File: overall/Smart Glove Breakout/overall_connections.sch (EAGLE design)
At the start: 3 parts

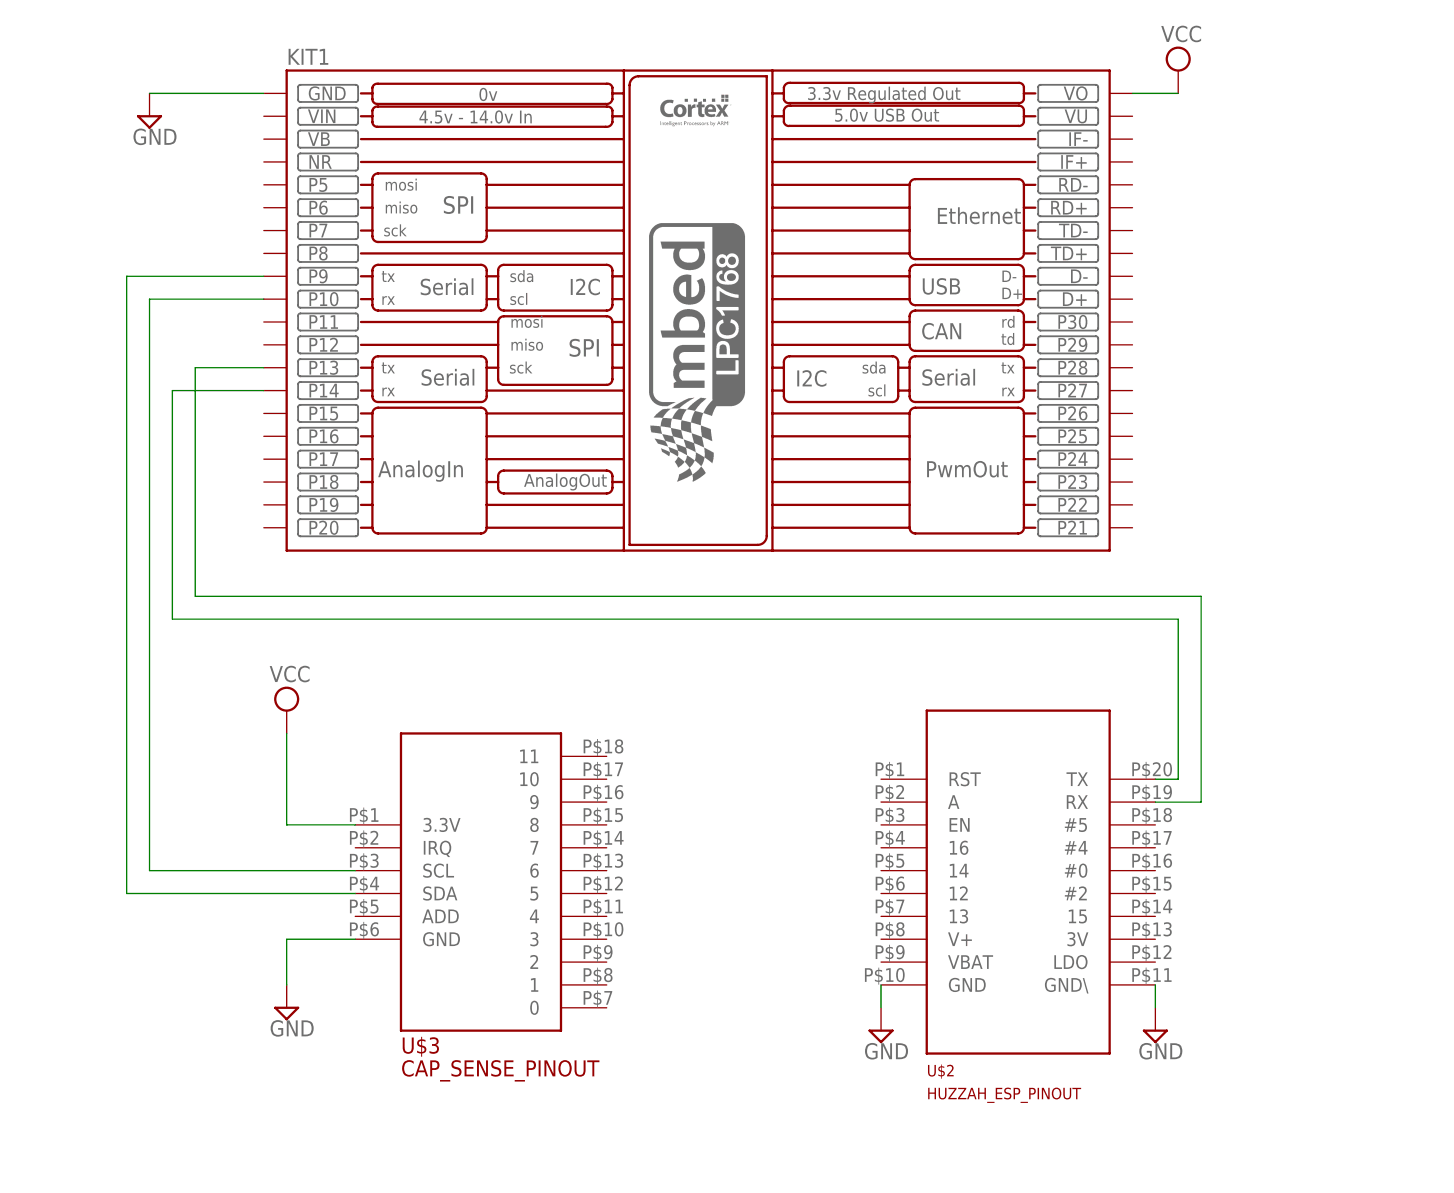
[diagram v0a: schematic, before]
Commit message: Revert "Started Board File"
This reverts commit 9f60d38fc5464a5e955318b8b377fab6b9ea1dbb.
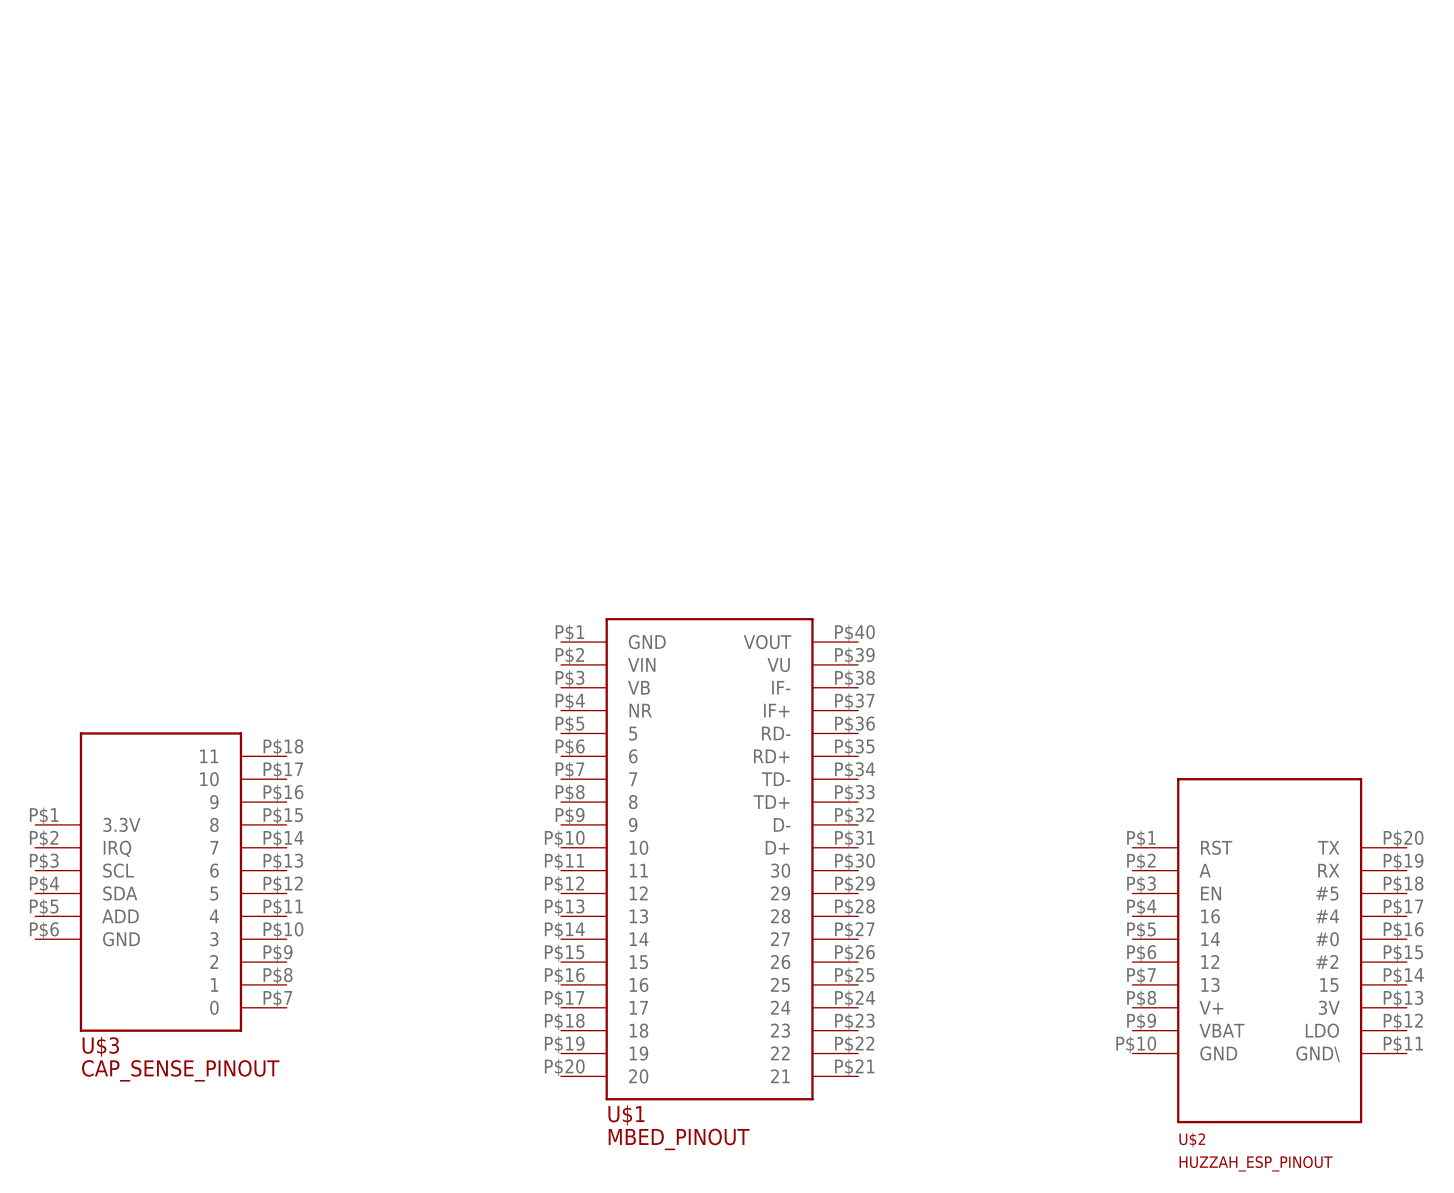
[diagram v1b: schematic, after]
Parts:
- removed KIT1: MBED_NXP_LPC1768, MBED_v2.1_avbotz:MBED_NXP_LPC1768
- added U$1: MBED_PINOUT, smart_glove_breakout:MBED_PINOUT
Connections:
- removed net GND: KIT1.GND, U$2.GND, U$2.GND\, U$3.GND
- removed net N$1: KIT1.P13, U$2.RX
- removed net N$2: KIT1.P14, U$2.TX
- removed net N$3: KIT1.P9, U$3.SDA
- removed net N$4: KIT1.P10, U$3.SCL
- removed net VCC: KIT1.VO, U$3.3.3V
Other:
- moved on the sheet: U$2, U$3
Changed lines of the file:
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@@
 <setting verticaltext="up"/>
 </settings>
-<grid distance="0.1" unitdist="inch" unit="inch" style="lines" multiple="1" display="no" altdistance="0.01" altunitdist="inch" altunit="inch"/>
+<grid distance="0.1" unitdist="inch" unit="inch" style="lines" multiple="1" display="yes" altdistance="0.01" altunitdist="inch" altunit="inch"/>
 <layers>
 <layer number="1" name="Top" color="4" fill="1" visible="no" active="no"/>
@@
 <layer number="97" name="Info" color="7" fill="1" visible="yes" active="yes"/>
 <layer number="98" name="Guide" color="6" fill="1" visible="yes" active="yes"/>
-<layer number="101" name="Hidden" color="15" fill="1" visible="no" active="yes"/>
-<layer number="102" name="Changes" color="12" fill="1" visible="no" active="yes"/>
 </layers>
 <schematic xreflabel="%F%N/%S.%C%R" xrefpart="/%S.%C%R">
@@
 </classes>
 <parts>
+<part name="U$1" library="smart_glove_breakout" deviceset="MBED_PINOUT" device=""/>
 <part name="U$2" library="smart_glove_breakout" deviceset="HUZZAH_ESP_PINOUT" device=""/>
 <part name="U$3" library="smart_glove_breakout" deviceset="CAP_SENSE_PINOUT" device=""/>
-<part name="KIT1" library="MBED_v2.1_avbotz" deviceset="MBED_NXP_LPC1768" device=""/>
-<part name="SUPPLY1" library="supply2" deviceset="GND" device=""/>
-<part name="SUPPLY2" library="supply2" deviceset="GND" device=""/>
-<part name="SUPPLY3" library="supply2" deviceset="VCC" device=""/>
-<part name="SUPPLY4" library="supply2" deviceset="VCC" device=""/>
-<part name="SUPPLY5" library="supply2" deviceset="GND" device=""/>
-<part name="SUPPLY6" library="supply2" deviceset="GND" device=""/>
 </parts>
 <sheets>
@@
 </plain>
 <instances>
-<instance part="U$2" gate="G$1" x="35.56" y="-7.62"/>
-<instance part="U$3" gate="G$1" x="-22.86" y="-12.7"/>
-<instance part="KIT1" gate="KIT" x="10.16" y="38.1"/>
-<instance part="SUPPLY1" gate="GND" x="-35.56" y="-40.64"/>
-<instance part="SUPPLY2" gate="GND" x="-50.8" y="58.42"/>
-<instance part="SUPPLY3" gate="G$1" x="-35.56" y="-7.62"/>
-<instance part="SUPPLY4" gate="G$1" x="63.5" y="63.5"/>
-<instance part="SUPPLY5" gate="GND" x="30.48" y="-43.18"/>
-<instance part="SUPPLY6" gate="GND" x="60.96" y="-43.18"/>
+<instance part="U$1" gate="G$1" x="0" y="0"/>
+<instance part="U$2" gate="G$1" x="63.5" y="-15.24"/>
+<instance part="U$3" gate="G$1" x="-58.42" y="-12.7"/>
 </instances>
 <busses>
 </busses>
 <nets>
-<net name="GND" class="0">
-<segment>
-<pinref part="U$3" gate="G$1" pin="GND"/>
-<wire x1="-27.94" y1="-33.02" x2="-35.56" y2="-33.02" width="0.1524" layer="91"/>
-<wire x1="-35.56" y1="-33.02" x2="-35.56" y2="-38.1" width="0.1524" layer="91"/>
-<pinref part="SUPPLY1" gate="GND" pin="GND"/>
-</segment>
-<segment>
-<pinref part="KIT1" gate="KIT" pin="GND"/>
-<pinref part="SUPPLY2" gate="GND" pin="GND"/>
-<wire x1="-38.1" y1="60.96" x2="-50.8" y2="60.96" width="0.1524" layer="91"/>
-</segment>
-<segment>
-<pinref part="U$2" gate="G$1" pin="GND"/>
-<pinref part="SUPPLY5" gate="GND" pin="GND"/>
-<wire x1="30.48" y1="-38.1" x2="30.48" y2="-40.64" width="0.1524" layer="91"/>
-</segment>
-<segment>
-<pinref part="U$2" gate="G$1" pin="GND\"/>
-<pinref part="SUPPLY6" gate="GND" pin="GND"/>
-<wire x1="60.96" y1="-38.1" x2="60.96" y2="-40.64" width="0.1524" layer="91"/>
-</segment>
-</net>
-<net name="VCC" class="0">
-<segment>
-<pinref part="U$3" gate="G$1" pin="3.3V"/>
-<wire x1="-27.94" y1="-20.32" x2="-35.56" y2="-20.32" width="0.1524" layer="91"/>
-<wire x1="-35.56" y1="-20.32" x2="-35.56" y2="-10.16" width="0.1524" layer="91"/>
-<pinref part="SUPPLY3" gate="G$1" pin="VCC"/>
-</segment>
-<segment>
-<pinref part="SUPPLY4" gate="G$1" pin="VCC"/>
-<pinref part="KIT1" gate="KIT" pin="VO"/>
-<wire x1="63.5" y1="60.96" x2="58.42" y2="60.96" width="0.1524" layer="91"/>
-</segment>
-</net>
-<net name="N$3" class="0">
-<segment>
-<pinref part="KIT1" gate="KIT" pin="P9"/>
-<wire x1="-38.1" y1="40.64" x2="-53.34" y2="40.64" width="0.1524" layer="91"/>
-<wire x1="-53.34" y1="40.64" x2="-53.34" y2="-27.94" width="0.1524" layer="91"/>
-<pinref part="U$3" gate="G$1" pin="SDA"/>
-<wire x1="-53.34" y1="-27.94" x2="-27.94" y2="-27.94" width="0.1524" layer="91"/>
-</segment>
-</net>
-<net name="N$4" class="0">
-<segment>
-<pinref part="KIT1" gate="KIT" pin="P10"/>
-<wire x1="-38.1" y1="38.1" x2="-50.8" y2="38.1" width="0.1524" layer="91"/>
-<wire x1="-50.8" y1="38.1" x2="-50.8" y2="-25.4" width="0.1524" layer="91"/>
-<pinref part="U$3" gate="G$1" pin="SCL"/>
-<wire x1="-50.8" y1="-25.4" x2="-27.94" y2="-25.4" width="0.1524" layer="91"/>
-</segment>
-</net>
-<net name="N$1" class="0">
-<segment>
-<pinref part="U$2" gate="G$1" pin="RX"/>
-<wire x1="66.04" y1="-17.78" x2="60.96" y2="-17.78" width="0.1524" layer="91"/>
-<wire x1="66.04" y1="-17.78" x2="66.04" y2="5.08" width="0.1524" layer="91"/>
-<wire x1="66.04" y1="5.08" x2="-45.72" y2="5.08" width="0.1524" layer="91"/>
-<wire x1="-45.72" y1="5.08" x2="-45.72" y2="30.48" width="0.1524" layer="91"/>
-<pinref part="KIT1" gate="KIT" pin="P13"/>
-<wire x1="-45.72" y1="30.48" x2="-38.1" y2="30.48" width="0.1524" layer="91"/>
-</segment>
-</net>
-<net name="N$2" class="0">
-<segment>
-<pinref part="U$2" gate="G$1" pin="TX"/>
-<wire x1="63.5" y1="-15.24" x2="60.96" y2="-15.24" width="0.1524" layer="91"/>
-<wire x1="63.5" y1="-15.24" x2="63.5" y2="2.54" width="0.1524" layer="91"/>
-<wire x1="63.5" y1="2.54" x2="-48.26" y2="2.54" width="0.1524" layer="91"/>
-<wire x1="-48.26" y1="2.54" x2="-48.26" y2="27.94" width="0.1524" layer="91"/>
-<pinref part="KIT1" gate="KIT" pin="P14"/>
-<wire x1="-48.26" y1="27.94" x2="-38.1" y2="27.94" width="0.1524" layer="91"/>
-</segment>
-</net>
 </nets>
 </sheet>
